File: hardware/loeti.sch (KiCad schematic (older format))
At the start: 47 parts, among them J0 USB_C_Receptacle_USB2.0, J1 STDC14, J2 AudioJack4, SW0 key2, U0 AP2204R-3.3, U1 STUSB4500QTR, U2 USBLC6-4SC6, U3 STM32F042K6Tx, U4 EA_DOGS104B-A, U5 VN7040AS, U6 ADS1118IDGS

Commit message: updates to bom initial software structure
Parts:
- J1: value STDC14 -> Samtec FTS-107-01-L-D
- R0, R1, R2, R3: value 2k37 -> 1k
- U1: symbol OtterIron_Devkit-rescue:STUSB4500-otter -> custom:STUSB4500
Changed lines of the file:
@@
 P 2500 10100
 F 0 "R1" H 2569 10146 50  0000 L CNN
-F 1 "2k37" H 2569 10055 50  0000 L CNN
+F 1 "1k" H 2569 10055 50  0000 L CNN
 F 2 "Capacitor_SMD:C_0603_1608Metric_Pad1.05x0.95mm_HandSolder" V 2430 10100 50  0001 C CNN
 F 3 "~" H 2500 10100 50  0001 C CNN
@@
 P 2800 10100
 F 0 "R2" H 2869 10146 50  0000 L CNN
-F 1 "2k37" H 2869 10055 50  0000 L CNN
+F 1 "1k" H 2869 10055 50  0000 L CNN
 F 2 "Capacitor_SMD:C_0603_1608Metric_Pad1.05x0.95mm_HandSolder" V 2730 10100 50  0001 C CNN
 F 3 "~" H 2800 10100 50  0001 C CNN
@@
 P 3100 10100
 F 0 "R3" H 3169 10146 50  0000 L CNN
-F 1 "2k37" H 3169 10055 50  0000 L CNN
+F 1 "1k" H 3169 10055 50  0000 L CNN
 F 2 "Capacitor_SMD:C_0603_1608Metric_Pad1.05x0.95mm_HandSolder" V 3030 10100 50  0001 C CNN
 F 3 "~" H 3100 10100 50  0001 C CNN
@@
 Wire Wire Line
 	3300 7650 3300 7200
-Connection ~ 2250 8650
-Connection ~ 2250 8550
-$Comp
-L OtterIron_Devkit-rescue:STUSB4500-otter U1
+$Comp
+L custom:STUSB4500 U1
 U 1 1 5CE79B83
 P 3050 8600
@@
 P 2100 8100
 F 0 "R0" H 2169 8146 50  0000 L CNN
-F 1 "2k37" H 2169 8055 50  0000 L CNN
+F 1 "1k" H 2169 8055 50  0000 L CNN
 F 2 "Capacitor_SMD:C_0603_1608Metric_Pad1.05x0.95mm_HandSolder" V 2030 8100 50  0001 C CNN
 F 3 "~" H 2100 8100 50  0001 C CNN
@@
 	0    1    1    0
 $EndComp
-Connection ~ 2250 8950
 Text GLabel 7750 3300 2    50   Input ~ 0
 PWM
@@
 P 4500 3750
 F 0 "J1" H 4500 3765 50  0000 C CNN
-F 1 "STDC14" H 4500 3674 50  0000 C CNN
+F 1 "Samtec FTS-107-01-L-D" H 4500 3674 50  0000 C CNN
 F 2 "Connector_PinHeader_1.27mm:PinHeader_2x07_P1.27mm_Vertical" H 4500 3750 50  0001 C CNN
 F 3 "" H 4500 3750 50  0001 C CNN

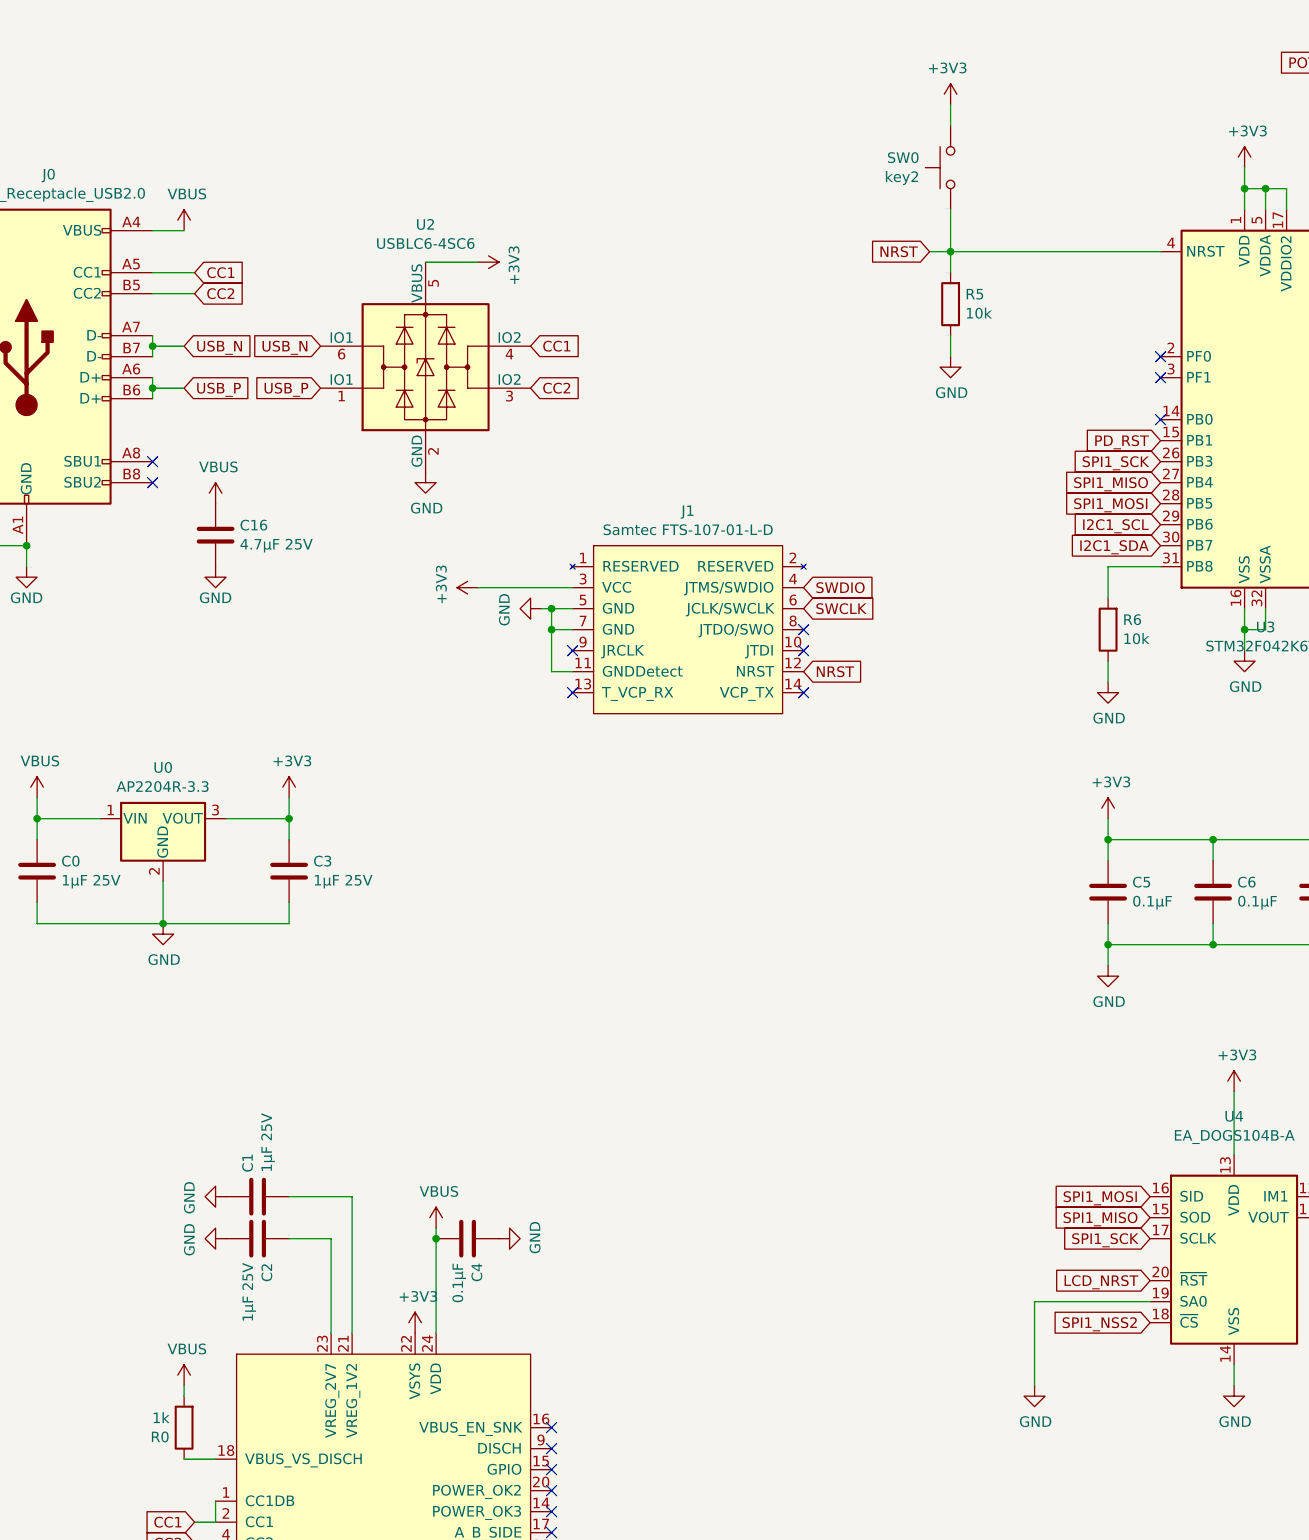
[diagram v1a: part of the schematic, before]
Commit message: usb pd working new layout
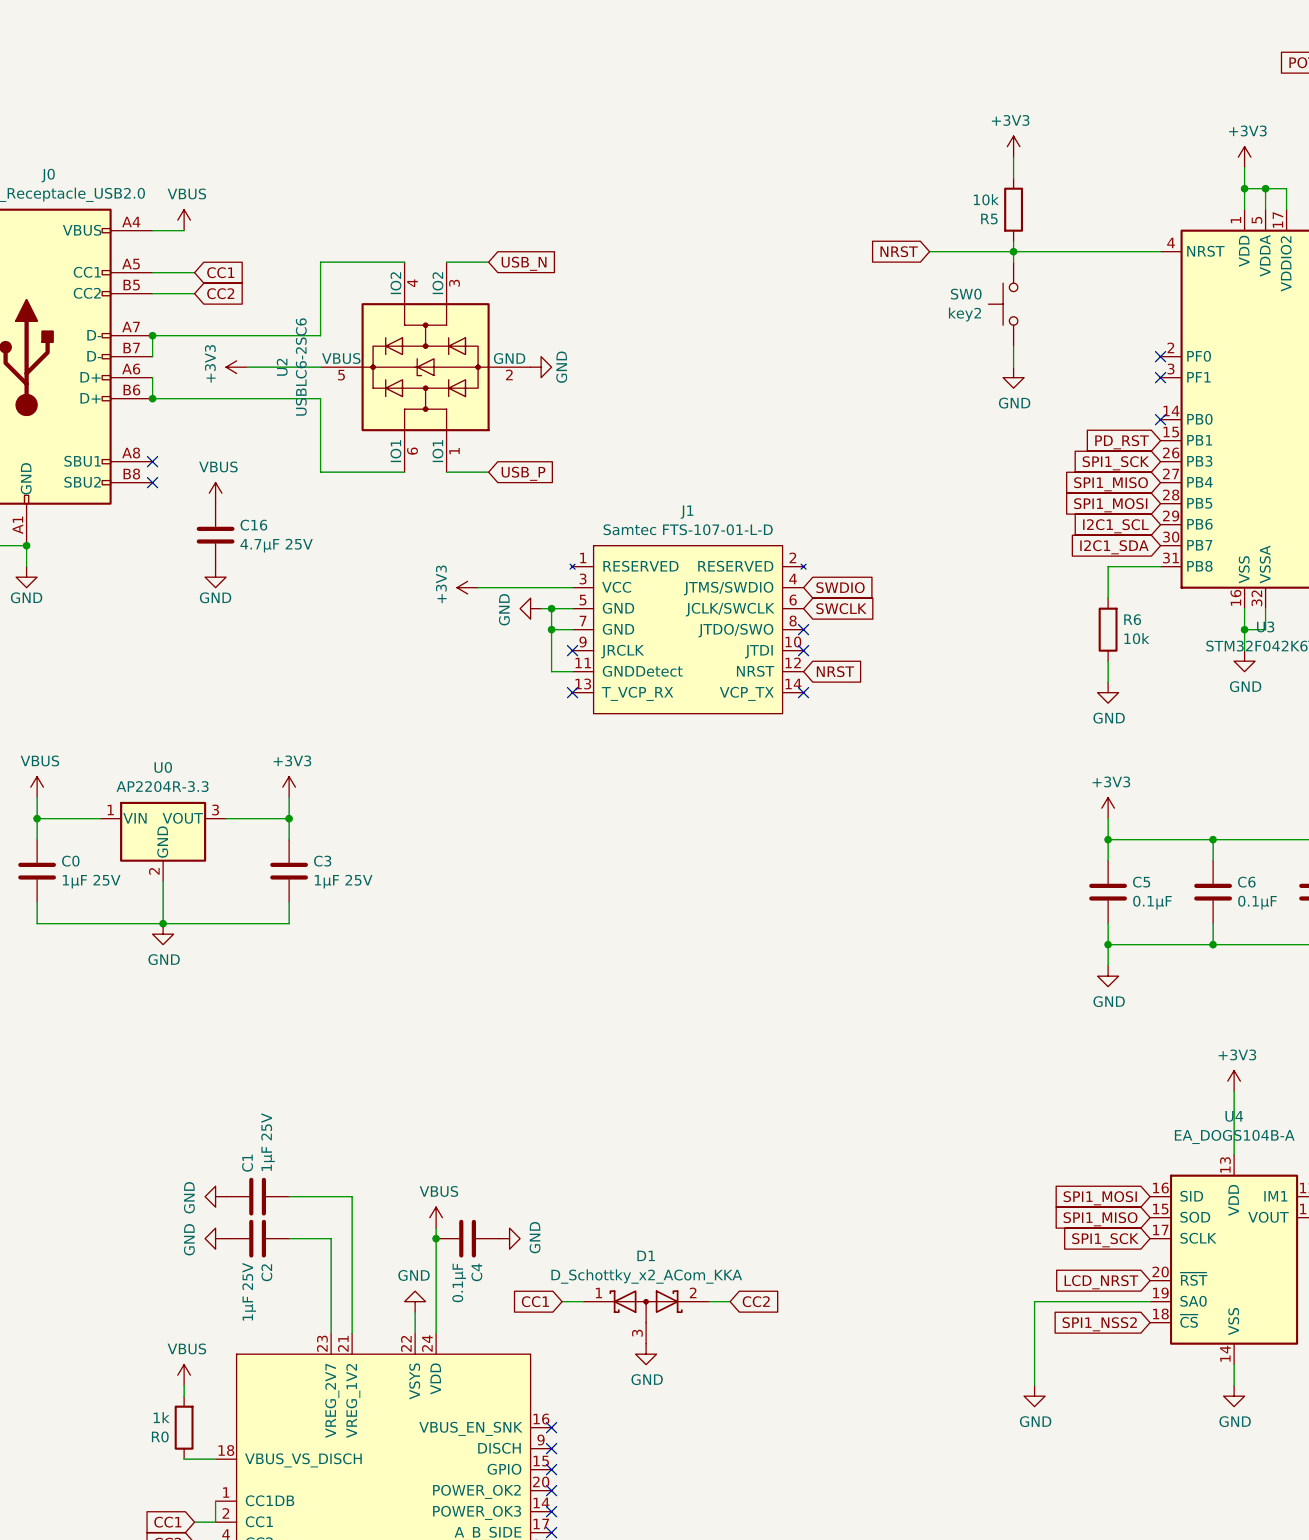
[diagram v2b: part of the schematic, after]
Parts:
- added D1: D_Schottky_x2_ACom_KKA, Package_TO_SOT_SMD:SOT-323_SC-70, symbol Device:D_Schottky_x2_ACom_KKA
- U2: value USBLC6-4SC6 -> USBLC6-2SC6
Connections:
- wire segments 154 -> 161
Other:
- moved on the sheet: R5, SW0
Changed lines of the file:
@@
 Connection ~ 2500 9850
 Wire Wire Line
-	5750 2900 5750 3000
+	6050 2950 6050 3050
 Wire Wire Line
 	7150 4300 7150 4400
@@
 Wire Wire Line
 	2500 9850 2500 9950
-Wire Wire Line
-	5750 2500 5750 2600
 $Comp
 L power:+3V3 #PWR024
@@
 L power:GND #PWR020
 U 1 1 5A9ADA03
-P 5750 3000
-F 0 "#PWR020" H 5750 2750 50  0001 C CNN
-F 1 "GND" H 5755 2827 50  0000 C CNN
-F 2 "" H 5750 3000 50  0001 C CNN
-F 3 "" H 5750 3000 50  0001 C CNN
-	1    5750 3000
+P 6050 3050
+F 0 "#PWR020" H 6050 2800 50  0001 C CNN
+F 1 "GND" H 6055 2877 50  0000 C CNN
+F 2 "" H 6050 3050 50  0001 C CNN
+F 3 "" H 6050 3050 50  0001 C CNN
+	1    6050 3050
 	1    0    0    -1
 $EndComp
@@
 Text GLabel 2150 8650 0    50   Input ~ 0
 CC2
-Text GLabel 2750 2950 0    50   Input ~ 0
-USB_N
-Text GLabel 3750 3150 2    50   Input ~ 0
-CC2
-$Comp
-L power:GND #PWR?
-U 1 1 5BDFF38B
-P 3250 3550
-AR Path="/588FB1D7/5BDFF38B" Ref="#PWR?"  Part="1"
-AR Path="/588FD270/5BDFF38B" Ref="#PWR?"  Part="1"
-AR Path="/5BDFF38B" Ref="#PWR013"  Part="1"
-F 0 "#PWR013" H 3250 3300 50  0001 C CNN
-F 1 "GND" H 3255 3377 50  0000 C CNN
-F 2 "" H 3250 3550 50  0001 C CNN
-F 3 "" H 3250 3550 50  0001 C CNN
-	1    3250 3550
-	1    0    0    -1
-$EndComp
-$Comp
-L power:+3V3 #PWR?
-U 1 1 5BDFF3DA
-P 3500 2550
-AR Path="/588FB1D7/5BDFF3DA" Ref="#PWR?"  Part="1"
-AR Path="/588FD270/5BDFF3DA" Ref="#PWR?"  Part="1"
-AR Path="/5BDFF3DA" Ref="#PWR016"  Part="1"
-F 0 "#PWR016" H 3500 2400 50  0001 C CNN
-F 1 "+3V3" H 3515 2723 50  0000 C CNN
-F 2 "" H 3500 2550 50  0001 C CNN
-F 3 "" H 3500 2550 50  0001 C CNN
-	1    3500 2550
-	0    1    1    0
-$EndComp
 Wire Wire Line
 	7950 5400 7950 5300
@@
 $EndComp
 $Comp
-L Power_Protection:USBLC6-2SC6 U2
-U 1 1 5BF3991B
-P 3250 3050
-F 0 "U2" H 3250 3728 50  0000 C CNN
-F 1 "USBLC6-4SC6" H 3250 3637 50  0000 C CNN
-F 2 "Package_TO_SOT_SMD:SOT-23-6" H 2500 3450 50  0001 C CNN
-F 3 "http://www2.st.com/resource/en/datasheet/CD00050750.pdf" H 3450 3400 50  0001 C CNN
-	1    3250 3050
-	1    0    0    -1
-$EndComp
-Text GLabel 2750 3150 0    50   Input ~ 0
-USB_P
-Text GLabel 3750 2950 2    50   Input ~ 0
-CC1
-$Comp
 L Switch:SW_Push SW0
 U 1 1 5C1295B7
-P 5750 2100
-F 0 "SW0" V 5704 2248 50  0000 L CNN
-F 1 "key2" V 5795 2248 50  0000 L CNN
-F 2 "Button_Switch_SMD:SW_SPST_PTS810" H 5750 2300 50  0001 C CNN
-F 3 "" H 5750 2300 50  0001 C CNN
-	1    5750 2100
+P 6050 2750
+F 0 "SW0" V 6004 2898 50  0000 L CNN
+F 1 "key2" V 6095 2898 50  0000 L CNN
+F 2 "Button_Switch_SMD:SW_SPST_PTS810" H 6050 2950 50  0001 C CNN
+F 3 "" H 6050 2950 50  0001 C CNN
+	1    6050 2750
 	0    -1   1    0
 $EndComp
@@
 L power:+3V3 #PWR019
 U 1 1 5C1295BE
-P 5750 1800
-F 0 "#PWR019" H 5750 1650 50  0001 C CNN
-F 1 "+3V3" H 5765 1973 50  0000 C CNN
-F 2 "" H 5750 1800 50  0001 C CNN
-F 3 "" H 5750 1800 50  0001 C CNN
-	1    5750 1800
+P 6050 2050
+F 0 "#PWR019" H 6050 1900 50  0001 C CNN
+F 1 "+3V3" H 6065 2223 50  0000 C CNN
+F 2 "" H 6050 2050 50  0001 C CNN
+F 3 "" H 6050 2050 50  0001 C CNN
+	1    6050 2050
 	-1   0    0    -1
 $EndComp
 Wire Wire Line
-	5750 1800 5750 1900
-Wire Wire Line
-	5750 2500 5750 2300
+	6050 2050 6050 2150
 Wire Wire Line
 	2100 2400 1950 2400
-Wire Wire Line
-	1950 2900 1950 2950
-Wire Wire Line
-	1950 2950 2100 2950
-Wire Wire Line
-	1950 3200 1950 3150
-Wire Wire Line
-	1950 3150 2100 3150
-Text GLabel 2100 2950 2    50   Input ~ 0
-USB_N
-Text GLabel 2100 3150 2    50   Input ~ 0
-USB_P
 $Comp
 L power:GND #PWR00
@@
 	1    2300 7000
 	0    1    1    0
-$EndComp
-$Comp
-L power:+3V3 #PWR010
-U 1 1 5CFBAA57
-P 3200 7650
-F 0 "#PWR010" H 3200 7500 50  0001 C CNN
-F 1 "+3V3" H 3215 7823 50  0000 C CNN
-F 2 "" H 3200 7650 50  0001 C CNN
-F 3 "" H 3200 7650 50  0001 C CNN
-	1    3200 7650
-	1    0    0    -1
 $EndComp
 $Comp
@@
 Text GLabel 9450 5050 0    50   Input ~ 0
 T+
-Connection ~ 5750 2500
 $Comp
 L Device:C C?
@@
 	1    0    0    -1
 $EndComp
-Wire Wire Line
-	5750 2500 6750 2500
 NoConn ~ 1950 3500
 NoConn ~ 1950 3600
@@
 	1    0    0    -1
 $EndComp
-Wire Wire Line
-	3500 2550 3250 2550
 Text GLabel 6750 3500 0    50   Input ~ 0
 SPI1_SCK
@@
 L Device:R R5
 U 1 1 5E824254
-P 5750 2750
-F 0 "R5" H 5680 2704 50  0000 R CNN
-F 1 "10k" H 5680 2795 50  0000 R CNN
-F 2 "Capacitor_SMD:C_0603_1608Metric_Pad1.05x0.95mm_HandSolder" V 5680 2750 50  0001 C CNN
-F 3 "~" H 5750 2750 50  0001 C CNN
-	1    5750 2750
-	-1   0    0    1
+P 6050 2300
+F 0 "R5" H 5980 2254 50  0000 R CNN
+F 1 "10k" H 5980 2345 50  0000 R CNN
+F 2 "Capacitor_SMD:C_0603_1608Metric_Pad1.05x0.95mm_HandSolder" V 5980 2300 50  0001 C CNN
+F 3 "~" H 6050 2300 50  0001 C CNN
+	1    6050 2300
+	1    0    0    -1
 $EndComp
 $Comp
@@
 Text GLabel 5650 2500 0    50   Input ~ 0
 NRST
-Wire Wire Line
-	5650 2500 5750 2500
 Text GLabel 7750 3800 2    50   Input ~ 0
 SWDIO
@@
 NoConn ~ 6750 3300
 NoConn ~ 7750 2500
-Connection ~ 1950 2950
-Wire Wire Line
-	1950 2950 1950 3000
-Connection ~ 1950 3150
-Wire Wire Line
-	1950 3150 1950 3100
 $Comp
 L custom:STDC14 J1
@@
 NoConn ~ 6750 3000
 NoConn ~ 6750 3100
+Wire Wire Line
+	5650 2500 6050 2500
+Wire Wire Line
+	6050 2450 6050 2500
+Connection ~ 6050 2500
+Wire Wire Line
+	6050 2500 6750 2500
+Wire Wire Line
+	6050 2500 6050 2550
+Text GLabel 3550 3550 2    50   Input ~ 0
+USB_P
+Text GLabel 3550 2550 2    50   Input ~ 0
+USB_N
+$Comp
+L Power_Protection:USBLC6-2SC6 U2
+U 1 1 5E962D2B
+P 3250 3050
+F 0 "U2" H 3250 3731 50  0000 C CNN
+F 1 "USBLC6-2SC6" H 3250 3640 50  0000 C CNN
+F 2 "Package_TO_SOT_SMD:SOT-23-6" H 2500 3450 50  0001 C CNN
+F 3 "http://www2.st.com/resource/en/datasheet/CD00050750.pdf" H 3450 3400 50  0001 C CNN
+	1    3250 3050
+	0    -1   -1   0
+$EndComp
+Wire Wire Line
+	1950 2900 1950 3000
+Wire Wire Line
+	1950 3100 1950 3200
+Wire Wire Line
+	3350 2550 3550 2550
+Wire Wire Line
+	3350 3550 3550 3550
+Wire Wire Line
+	3150 3550 2750 3550
+Wire Wire Line
+	2750 3550 2750 3200
+Wire Wire Line
+	2750 3200 1950 3200
+Connection ~ 1950 3200
+Wire Wire Line
+	1950 2900 2750 2900
+Wire Wire Line
+	2750 2900 2750 2550
+Wire Wire Line
+	2750 2550 3150 2550
+Connection ~ 1950 2900
+Wire Wire Line
+	2400 3050 2750 3050
+$Comp
+L power:GND #PWR0104
+U 1 1 5E9A5EA0
+P 3750 3050
+F 0 "#PWR0104" H 3750 2800 50  0001 C CNN
+F 1 "GND" H 3750 2900 50  0000 C CNN
+F 2 "" H 3750 3050 50  0001 C CNN
+F 3 "" H 3750 3050 50  0001 C CNN
+	1    3750 3050
+	0    -1   -1   0
+$EndComp
+$Comp
+L Device:D_Schottky_x2_ACom_KKA D1
+U 1 1 5E9BD548
+P 4300 7500
+F 0 "D1" H 4300 7716 50  0000 C CNN
+F 1 "D_Schottky_x2_ACom_KKA" H 4300 7625 50  0000 C CNN
+F 2 "Package_TO_SOT_SMD:SOT-323_SC-70" H 4300 7500 50  0001 C CNN
+F 3 "~" H 4300 7500 50  0001 C CNN
+	1    4300 7500
+	1    0    0    -1
+$EndComp
+$Comp
+L power:GND #PWR0103
+U 1 1 5E9C1638
+P 4300 7700
+F 0 "#PWR0103" H 4300 7450 50  0001 C CNN
+F 1 "GND" H 4305 7527 50  0000 C CNN
+F 2 "" H 4300 7700 50  0001 C CNN
+F 3 "" H 4300 7700 50  0001 C CNN
+	1    4300 7700
+	1    0    0    -1
+$EndComp
+Text GLabel 3900 7500 0    50   Input ~ 0
+CC1
+Text GLabel 4700 7500 2    50   Input ~ 0
+CC2
+Wire Wire Line
+	4700 7500 4600 7500
+Wire Wire Line
+	3900 7500 4000 7500
+$Comp
+L power:+3V3 #PWR0105
+U 1 1 5E9E2C0E
+P 2400 3050
+F 0 "#PWR0105" H 2400 2900 50  0001 C CNN
+F 1 "+3V3" H 2415 3223 50  0000 C CNN
+F 2 "" H 2400 3050 50  0001 C CNN
+F 3 "" H 2400 3050 50  0001 C CNN
+	1    2400 3050
+	0    -1   -1   0
+$EndComp
+$Comp
+L power:GND #PWR?
+U 1 1 5EA3EF18
+P 3200 7550
+F 0 "#PWR?" H 3200 7300 50  0001 C CNN
+F 1 "GND" H 3205 7377 50  0000 C CNN
+F 2 "" H 3200 7550 50  0001 C CNN
+F 3 "" H 3200 7550 50  0001 C CNN
+	1    3200 7550
+	-1   0    0    1
+$EndComp
+Wire Wire Line
+	3200 7550 3200 7650
 $EndSCHEMATC

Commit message: fully working revision
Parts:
- removed C10: 0.1μF, Capacitor_SMD:C_0603_1608Metric_Pad1.05x0.95mm_HandSolder, symbol Device:C
- removed R7, R8: 10k, Capacitor_SMD:C_0603_1608Metric_Pad1.05x0.95mm_HandSolder, symbol Device:R
- removed U5: VN7040AS, Package_SO:SO-8_3.9x4.9mm_P1.27mm, symbol custom:VN7040AS
- added C17: EEU-FR1V471L, custom:CP_Radial_D8.0mm_P3.50mm_HOR, symbol Device:CP
- added D2: ESDA25P35, Diode_SMD:D_0603_1608Metric_Pad1.05x0.95mm_HandSolder, symbol Device:D_Schottky
- added Q1, Q2: BC817, Package_TO_SOT_SMD:SOT-23, symbol Transistor_BJT:BC817
- added Q3: BC807, Package_TO_SOT_SMD:SOT-23, symbol Transistor_BJT:BC807
- added Q4: Si4825DDY, DMG4435SSS, IRF9393PbF, Package_SO:SO-8_3.9x4.9mm_P1.27mm, symbol custom:SI4425FDY
- added R12, R13: 1k, Resistor_SMD:R_0603_1608Metric_Pad1.05x0.95mm_HandSolder, symbol Device:R
- added R14: 20, Resistor_SMD:R_0603_1608Metric_Pad1.05x0.95mm_HandSolder, symbol Device:R
- added SW2, SW3: SW_SPST, custom:Omron-B3AL, symbol Switch:SW_SPST
- C13: renamed from C12; value 0.01μF -> 0.1μF
- C15: renamed from C14; value 0.01μF -> 0.1μF
- D1: value D_Schottky_x2_ACom_KKA -> ESDA25W
- R1: renamed from R0; footprint Capacitor_SMD:C_0603_1608Metric_Pad1.05x0.95mm_HandSolder -> Resistor_SMD:R_0603_1608Metric_Pad1.05x0.95mm_HandSolder
- R10: renamed from R11; footprint Capacitor_SMD:C_0603_1608Metric_Pad1.05x0.95mm_HandSolder -> Resistor_SMD:R_0603_1608Metric_Pad1.05x0.95mm_HandSolder
- R11: renamed from R12; footprint Capacitor_SMD:C_0603_1608Metric_Pad1.05x0.95mm_HandSolder -> Resistor_SMD:R_0603_1608Metric_Pad1.05x0.95mm_HandSolder
- R2: renamed from R1; footprint Capacitor_SMD:C_0603_1608Metric_Pad1.05x0.95mm_HandSolder -> Resistor_SMD:R_0603_1608Metric_Pad1.05x0.95mm_HandSolder
- R3: renamed from R2; footprint Capacitor_SMD:C_0603_1608Metric_Pad1.05x0.95mm_HandSolder -> Resistor_SMD:R_0603_1608Metric_Pad1.05x0.95mm_HandSolder
- R4: renamed from R3; footprint Capacitor_SMD:C_0603_1608Metric_Pad1.05x0.95mm_HandSolder -> Resistor_SMD:R_0603_1608Metric_Pad1.05x0.95mm_HandSolder
- R5: renamed from R4; footprint Capacitor_SMD:C_0603_1608Metric_Pad1.05x0.95mm_HandSolder -> Resistor_SMD:R_0603_1608Metric_Pad1.05x0.95mm_HandSolder
- R6: renamed from R5; footprint Capacitor_SMD:C_0603_1608Metric_Pad1.05x0.95mm_HandSolder -> Resistor_SMD:R_0603_1608Metric_Pad1.05x0.95mm_HandSolder
- R7: renamed from R6; footprint Capacitor_SMD:C_0603_1608Metric_Pad1.05x0.95mm_HandSolder -> Resistor_SMD:R_0603_1608Metric_Pad1.05x0.95mm_HandSolder
- R8: renamed from R9; footprint Capacitor_SMD:C_0603_1608Metric_Pad1.05x0.95mm_HandSolder -> Resistor_SMD:R_0603_1608Metric_Pad1.05x0.95mm_HandSolder
- R9: renamed from R10; footprint Capacitor_SMD:C_0603_1608Metric_Pad1.05x0.95mm_HandSolder -> Resistor_SMD:R_0603_1608Metric_Pad1.05x0.95mm_HandSolder
- U6: footprint Package_DFN_QFN:DFN-10-1EP_3x3mm_P0.5mm_EP1.75x2.7mm -> Package_SO:VSSOP-10_3x3mm_P0.5mm
- renumbered C0 to C1, C9 to C10, C8 to C11, C11 to C12, C13 to C14, C15 to C16, C16 to C2, C1 to C3, C2 to C4, C3 to C5, C4 to C6, C5 to C7, C6 to C8, C7 to C9, J0 to J1, J1 to J2, J2 to J3, SW0 to SW1, U0 to U1, U1 to U2, U2 to U3, U3 to U5
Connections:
- net labels removed: ADC_IN1, CV_SENSE, SEn
- wire segments 161 -> 180
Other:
- note added: "20 V Vgs, 20 V Vds minimum requirement for PMOS"
- note added: "LCD"
- note added: "MCU and programming header"
- note added: "Power switch"
- note added: "Thermocouple ADC"
- moved on the sheet: C1, C10, C11, C12, C13, C14, C15, C16, C2, C3, C4, C5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
